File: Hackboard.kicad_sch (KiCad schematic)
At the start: 70 parts, among them J1 Conn_01x23_Socket, J2 Micro_SD_Card, J3 Conn_01x31_Socket, J4 Conn_01x08_Socket, J5 Conn_02x02_Counter_Clockwise, J6 USB_C_Receptacle_USB2.0_16P, J7 Barrel_Jack_Switch, Q1 NMOS, Q2 NMOS, Q3 NMOS, SW1 SW_SPST, U1 NCP164CSN330T1G, U2 AP63205WU, U3 STM32L476RGT6, U4 74LVC4245APW, U5 74LVC4245APW, U6 74LVC4245APW, U7 USBLC6-2SC6, U8 74LVC4245APW, U9 74LVC4245APW

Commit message: Finish board layout
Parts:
- removed J5: Conn_02x02_Counter_Clockwise, Connector_PinHeader_2.54mm:PinHeader_2x02_P2.54mm_Vertical, symbol Connector_Generic:Conn_02x02_Counter_Clockwise
- added C18: 0.1uF, Capacitor_SMD:C_0603_1608Metric, symbol Device:C
- added J5: Conn_01x02_Pin, Connector_PinHeader_2.54mm:PinHeader_1x02_P2.54mm_Vertical, symbol Connector:Conn_01x02_Pin
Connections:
- net +3V3: now also C18.1
- net GND: now also C18.2
- net SW_SWCLK: now also J5.2 (Pin_2)
- net SW_SWDIO: now also J5.1 (Pin_1)
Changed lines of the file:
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@@
 		)
 	)
+	(wire
+		(pts
+			(xy 170.18 181.61) (xy 170.18 182.88)
+		)
+		(stroke
+			(width 0)
+			(type default)
+		)
+	)
 	(polyline
 		(pts
@@
 	(wire
 		(pts
-			(xy 31.75 43.18) (xy 34.29 43.18)
+			(xy 170.18 172.72) (xy 170.18 173.99)
 		)
 		(stroke
@@
 	(wire
 		(pts
-			(xy 199.39 160.02) (xy 198.12 160.02)
+			(xy 31.75 43.18) (xy 34.29 43.18)
 		)
 		(stroke
@@
 		)
 	)
-	(global_label "SD_SCK_24"
-		(shape bidirectional)
-		(at 198.12 157.48 0)
-		(fields_autoplaced yes)
-		(effects
-			(font
-				(size 1.27 1.27)
-			)
-			(justify left)
-		)
-		(property "Intersheetrefs" "${INTERSHEET_REFS}"
-			(at 212.7997 157.48 0)
-			(effects
-				(font
-					(size 1.27 1.27)
-				)
-				(justify left)
-				(hide yes)
-			)
-		)
-	)
 	(global_label "PWM_13_O"
 		(shape bidirectional)
@@
 	)
 	(symbol
+		(lib_id "power:GND")
+		(at 170.18 182.88 0)
+		(mirror y)
+		(unit 1)
+		(exclude_from_sim no)
+		(in_bom yes)
+		(on_board yes)
+		(dnp no)
+		(fields_autoplaced yes)
+		(property "Reference" "#PWR075"
+			(at 170.18 189.23 0)
+			(effects
+				(font
+					(size 1.27 1.27)
+				)
+				(hide yes)
+			)
+		)
+		(property "Value" "GND"
+			(at 170.18 187.96 0)
+			(effects
+				(font
+					(size 1.27 1.27)
+				)
+				(hide yes)
+			)
+		)
+		(property "Footprint" ""
+			(at 170.18 182.88 0)
+			(effects
+				(font
+					(size 1.27 1.27)
+				)
+				(hide yes)
+			)
+		)
+		(property "Datasheet" ""
+			(at 170.18 182.88 0)
+			(effects
+				(font
+					(size 1.27 1.27)
+				)
+				(hide yes)
+			)
+		)
+		(property "Description" "Power symbol creates a global label with name \"GND\" , ground"
+			(at 170.18 182.88 0)
+			(effects
+				(font
+					(size 1.27 1.27)
+				)
+				(hide yes)
+			)
+		)
+		(pin "1"
+		)
+		(instances
+			(project "Hackboard"
+				(path "/478098fb-f4b2-4694-bef3-d53baad1e8cf"
+					(reference "#PWR075")
+					(unit 1)
+				)
+			)
+		)
+	)
+	(symbol
 		(lib_id "power:+3V3")
 		(at 120.65 77.47 90)
@@
 	)
 	(symbol
-		(lib_id "power:GND")
-		(at 199.39 160.02 0)
-		(unit 1)
-		(exclude_from_sim no)
-		(in_bom yes)
-		(on_board yes)
-		(dnp no)
-		(fields_autoplaced yes)
-		(property "Reference" "#PWR049"
-			(at 199.39 166.37 0)
-			(effects
-				(font
-					(size 1.27 1.27)
-				)
-				(hide yes)
-			)
-		)
-		(property "Value" "GND"
-			(at 199.39 165.1 0)
-			(effects
-				(font
-					(size 1.27 1.27)
-				)
-				(hide yes)
-			)
-		)
-		(property "Footprint" ""
-			(at 199.39 160.02 0)
-			(effects
-				(font
-					(size 1.27 1.27)
-				)
-				(hide yes)
-			)
-		)
-		(property "Datasheet" ""
-			(at 199.39 160.02 0)
-			(effects
-				(font
-					(size 1.27 1.27)
-				)
-				(hide yes)
-			)
-		)
-		(property "Description" "Power symbol creates a global label with name \"GND\" , ground"
-			(at 199.39 160.02 0)
-			(effects
-				(font
-					(size 1.27 1.27)
-				)
-				(hide yes)
-			)
-		)
-		(pin "1"
-		)
-		(instances
-			(project "Hackboard"
-				(path "/478098fb-f4b2-4694-bef3-d53baad1e8cf"
-					(reference "#PWR049")
-					(unit 1)
-				)
-			)
-		)
-	)
-	(symbol
 		(lib_id "power:+3V3")
 		(at 142.24 170.18 270)
@@
 	)
 	(symbol
-		(lib_id "Connector_Generic:Conn_02x02_Counter_Clockwise")
-		(at 190.5 157.48 0)
-		(unit 1)
-		(exclude_from_sim no)
-		(in_bom yes)
-		(on_board yes)
-		(dnp no)
-		(property "Reference" "J5"
-			(at 190.5 154.178 0)
-			(effects
-				(font
-					(size 1.27 1.27)
-				)
-			)
-		)
-		(property "Value" "Conn_02x02_Counter_Clockwise"
-			(at 191.77 153.67 0)
-			(effects
-				(font
-					(size 1.27 1.27)
-				)
-				(hide yes)
-			)
-		)
-		(property "Footprint" "Connector_PinHeader_2.54mm:PinHeader_2x02_P2.54mm_Vertical"
-			(at 190.5 157.48 0)
-			(effects
-				(font
-					(size 1.27 1.27)
-				)
-				(hide yes)
-			)
-		)
-		(property "Datasheet" "~"
-			(at 190.5 157.48 0)
-			(effects
-				(font
-					(size 1.27 1.27)
-				)
-				(hide yes)
-			)
-		)
-		(property "Description" "Generic connector, double row, 02x02, counter clockwise pin numbering scheme (similar to DIP package numbering), script generated (kicad-library-utils/schlib/autogen/connector/)"
-			(at 190.5 157.48 0)
-			(effects
-				(font
-					(size 1.27 1.27)
-				)
-				(hide yes)
-			)
-		)
-		(pin "4"
-		)
-		(pin "2"
-		)
-		(pin "3"
-		)
-		(pin "1"
-		)
-		(instances
-			(project "Hackboard"
-				(path "/478098fb-f4b2-4694-bef3-d53baad1e8cf"
-					(reference "J5")
-					(unit 1)
-				)
-			)
-		)
-	)
-	(symbol
 		(lib_id "power:+3V3")
 		(at 72.39 172.72 0)
@@
 	)
 	(symbol
+		(lib_id "Connector:Conn_01x02_Pin")
+		(at 190.5 160.02 180)
+		(unit 1)
+		(exclude_from_sim no)
+		(in_bom yes)
+		(on_board yes)
+		(dnp no)
+		(fields_autoplaced yes)
+		(property "Reference" "J5"
+			(at 191.77 157.4799 0)
+			(effects
+				(font
+					(size 1.27 1.27)
+				)
+				(justify right)
+			)
+		)
+		(property "Value" "Conn_01x02_Pin"
+			(at 191.77 160.0199 0)
+			(effects
+				(font
+					(size 1.27 1.27)
+				)
+				(justify right)
+				(hide yes)
+			)
+		)
+		(property "Footprint" "Connector_PinHeader_2.54mm:PinHeader_1x02_P2.54mm_Vertical"
+			(at 190.5 160.02 0)
+			(effects
+				(font
+					(size 1.27 1.27)
+				)
+				(hide yes)
+			)
+		)
+		(property "Datasheet" "~"
+			(at 190.5 160.02 0)
+			(effects
+				(font
+					(size 1.27 1.27)
+				)
+				(hide yes)
+			)
+		)
+		(property "Description" "Generic connector, single row, 01x02, script generated"
+			(at 190.5 160.02 0)
+			(effects
+				(font
+					(size 1.27 1.27)
+				)
+				(hide yes)
+			)
+		)
+		(pin "2"
+		)
+		(pin "1"
+		)
+		(instances
+			(project "Hackboard"
+				(path "/478098fb-f4b2-4694-bef3-d53baad1e8cf"
+					(reference "J5")
+					(unit 1)
+				)
+			)
+		)
+	)
+	(symbol
 		(lib_id "Device:FerriteBead")
 		(at 114.3 20.32 90)
@@
 	(symbol
 		(lib_id "Device:C")
+		(at 170.18 177.8 0)
+		(mirror y)
+		(unit 1)
+		(exclude_from_sim no)
+		(in_bom yes)
+		(on_board yes)
+		(dnp no)
+		(property "Reference" "C18"
+			(at 163.83 172.72 0)
+			(effects
+				(font
+					(size 1.27 1.27)
+				)
+				(justify right)
+			)
+		)
+		(property "Value" "0.1uF"
+			(at 163.83 174.752 0)
+			(effects
+				(font
+					(size 1.27 1.27)
+				)
+				(justify right)
+			)
+		)
+		(property "Footprint" "Capacitor_SMD:C_0603_1608Metric"
+			(at 169.2148 181.61 0)
+			(effects
+				(font
+					(size 1.27 1.27)
+				)
+				(hide yes)
+			)
+		)
+		(property "Datasheet" "~"
+			(at 170.18 177.8 0)
+			(effects
+				(font
+					(size 1.27 1.27)
+				)
+				(hide yes)
+			)
+		)
+		(property "Description" "Unpolarized capacitor"
+			(at 170.18 177.8 0)
+			(effects
+				(font
+					(size 1.27 1.27)
+				)
+				(hide yes)
+			)
+		)
+		(pin "2"
+		)
+		(pin "1"
+		)
+		(instances
+			(project "Hackboard"
+				(path "/478098fb-f4b2-4694-bef3-d53baad1e8cf"
+					(reference "C18")
+					(unit 1)
+				)
+			)
+		)
+	)
+	(symbol
+		(lib_id "Device:C")
 		(at 85.09 22.86 0)
 		(unit 1)
@@
 					(unit 1)
 				)
+			)
+		)
+	)
+	(symbol
+		(lib_id "power:+3V3")
+		(at 170.18 172.72 0)
+		(unit 1)
+		(exclude_from_sim no)
+		(in_bom yes)
+		(on_board yes)
+		(dnp no)
+		(property "Reference" "#PWR049"
+			(at 170.18 176.53 0)
+			(effects
+				(font
+					(size 1.27 1.27)
+				)
+				(hide yes)
+			)
+		)
+		(property "Value" "+3V3"
+			(at 169.926 168.656 0)
+			(effects
+				(font
+					(size 1.27 1.27)
+				)
+			)
+		)
+		(property "Footprint" ""
+			(at 170.18 172.72 0)
+			(effects
+				(font
+					(size 1.27 1.27)
+				)
+				(hide yes)
+			)
+		)
+		(property "Datasheet" ""
+			(at 170.18 172.72 0)
+			(effects
+				(font
+					(size 1.27 1.27)
+				)
+				(hide yes)
+			)
+		)
+		(property "Description" "Power symbol creates a global label with name \"+3V3\""
+			(at 170.18 172.72 0)
+			(effects
+				(font
+					(size 1.27 1.27)
+				)
+				(hide yes)
+			)
+		)
+		(pin "1"
+		)
+		(instances
+			(project "Hackboard"
+				(path "/478098fb-f4b2-4694-bef3-d53baad1e8cf"
+					(reference "#PWR049")
+					(unit 1)
+				)

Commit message: Adjust pinout
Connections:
- net +3V3: no longer Q2.2 (G), Q3.2 (G), R10.2, R11.1
- net PWM_27: now also U3.59 (PB7); no longer U3.58 (PB6)
- net PWM_27_O: now also JP2.1 (A); no longer U5.6 (A3)
- net PWM_28: now also U3.58 (PB6); no longer U3.59 (PB7)
- net PWM_28_O: now also U5.7 (A4); no longer JP2.1 (A)
- net SD_SCK_24: no longer U3.55 (PB3), U5.19 (B0)
- net VDDA: now also Q2.2 (G), Q3.2 (G), R10.2, R11.1
- net at JP2.2 (B): now also U5.6 (A3); no longer U5.7 (A4)
- net CAN_RX_29 renamed CAN_RX_26
- net CAN_RX_26: now also U5.17 (B2); no longer U5.14 (B5)
- net CAN_RX_29_O renamed PWM_29_O
- net CAN_TX_30 renamed CAN_TX_25
- net CAN_TX_25: now also U5.18 (B1); no longer U5.13 (B6)
- net CAN_TX_30_O renamed PWM_30_O
- net GPIO_31 renamed GPIO_24
- net GPIO_24: now also U5.19 (B0); no longer U5.12 (B7)
- net GPIO_31_O renamed SD_SCK_31_O
- net PWM_25 renamed PWM_30
- net PWM_30: now also U5.13 (B6); no longer U5.18 (B1)
- net PWM_25_O renamed CAN_TX_25_O
- net PWM_26 renamed PWM_29
- net PWM_29: now also U5.14 (B5); no longer U5.17 (B2)
- net PWM_26_O renamed CAN_RX_26_O
- net SD_SCK_24_O renamed GPIO_24_O
- new net SD_SCK_31: U3.55 (PB3), U5.12 (B7)
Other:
- moved on the sheet: JP2

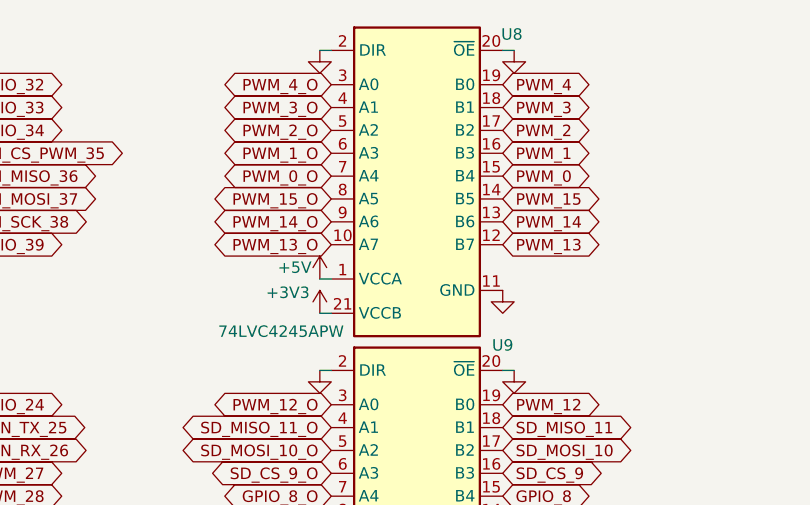
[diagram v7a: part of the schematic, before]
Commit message: Finish tracing most digital lines
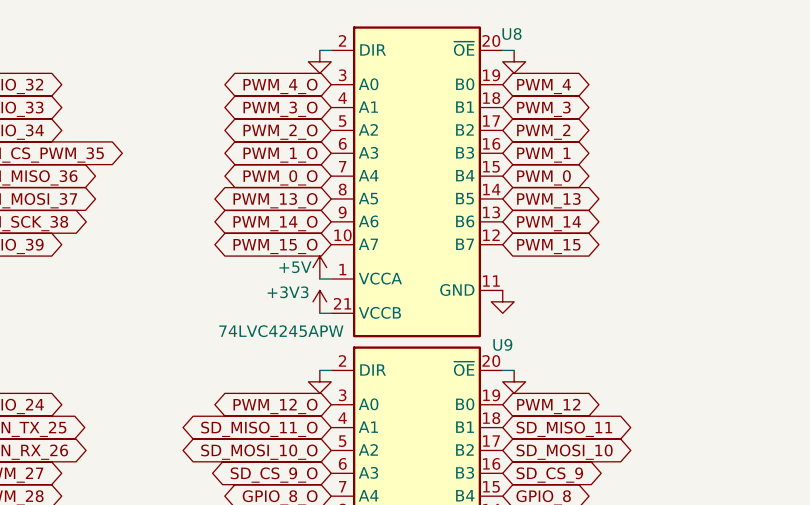
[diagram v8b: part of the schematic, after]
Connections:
- net PWM_13: now also U8.14 (B5); no longer U8.12 (B7)
- net PWM_13_O: now also U8.8 (A5); no longer U8.10 (A7)
- net PWM_15: now also U8.12 (B7); no longer U8.14 (B5)
- net PWM_15_O: now also U8.10 (A7); no longer U8.8 (A5)
